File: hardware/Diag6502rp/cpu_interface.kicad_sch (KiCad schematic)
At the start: 23 parts, among them J10 Conn_01x20_PinHeader, J11 Conn_01x20_PinHeader, J6 Conn_02x20_Counter_Clockwise, U4 TXS0108EPWR, U5 TXS0108EPWR, U6 TXS0108EPWR, U7 TXS0108EPWR, U8 TXS0108EPWR

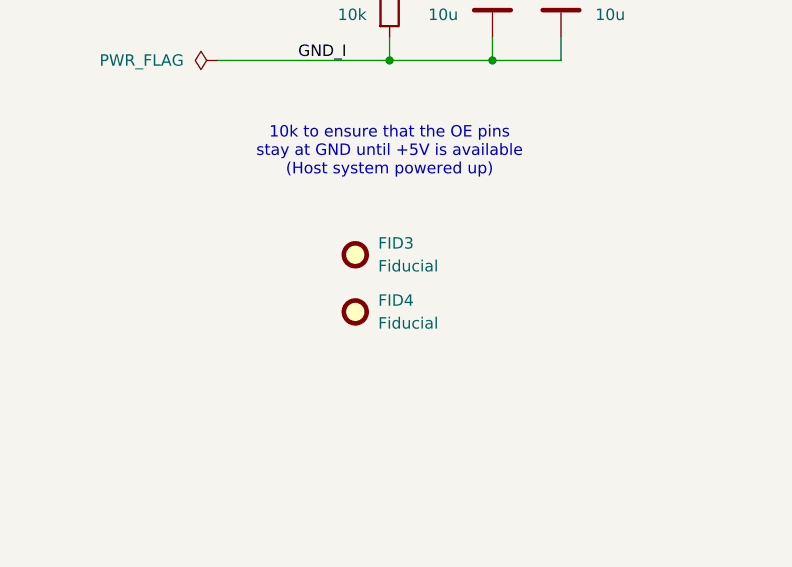
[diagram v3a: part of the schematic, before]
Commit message: More via separation and transfer vias
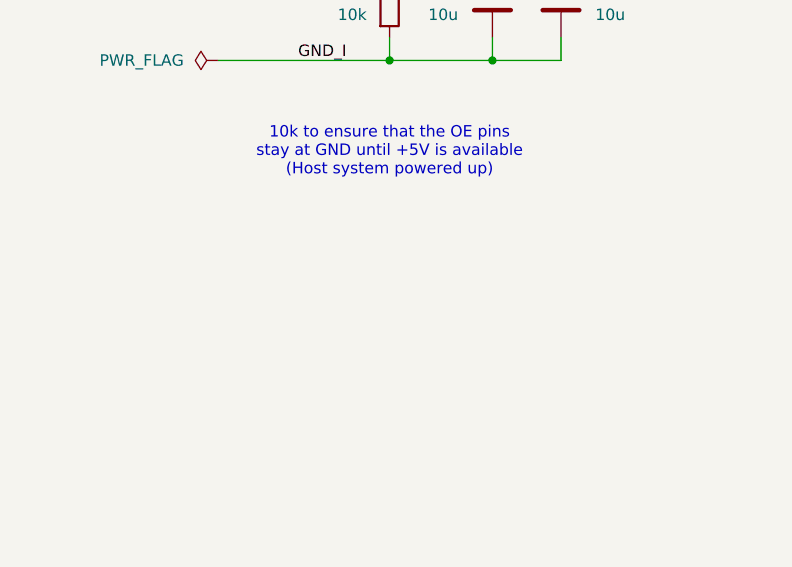
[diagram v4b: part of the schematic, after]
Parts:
- removed FID3, FID4: Fiducial, Fiducial:Fiducial_1mm_Mask2mm, symbol Mechanical:Fiducial
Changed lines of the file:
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@@
-	)
-	(symbol
-		(lib_id "Mechanical:Fiducial")
-		(at 231.14 149.86 0)
-		(unit 1)
-		(exclude_from_sim no)
-		(in_bom no)
-		(on_board yes)
-		(dnp no)
-		(fields_autoplaced yes)
-		(property "Reference" "FID3"
-			(at 233.68 148.5899 0)
-			(effects
-				(font
-					(size 1.27 1.27)
-				)
-				(justify left)
-			)
-		)
-		(property "Value" "Fiducial"
-			(at 233.68 151.1299 0)
-			(effects
-				(font
-					(size 1.27 1.27)
-				)
-				(justify left)
-			)
-		)
-		(property "Footprint" "Fiducial:Fiducial_1mm_Mask2mm"
-			(at 231.14 149.86 0)
-			(effects
-				(font
-					(size 1.27 1.27)
-				)
-				(hide yes)
-			)
-		)
-		(property "Datasheet" "~"
-			(at 231.14 149.86 0)
-			(effects
-				(font
-					(size 1.27 1.27)
-				)
-				(hide yes)
-			)
-		)
-		(property "Description" "Fiducial Marker"
-			(at 231.14 149.86 0)
-			(effects
-				(font
-					(size 1.27 1.27)
-				)
-				(hide yes)
-			)
-		)
-		(instances
-			(project ""
-				(path "/2439caa5-1b7d-40de-b309-64357b0b1cd3/c003db24-4bd6-49ad-8fb6-68dae2466627"
-					(reference "FID3")
-					(unit 1)
-				)
-			)
-		)
 	)
 	(symbol
@@
 					(unit 1)
 				)
-			)
-		)
-	)
-	(symbol
-		(lib_id "Mechanical:Fiducial")
-		(at 231.14 156.21 0)
-		(unit 1)
-		(exclude_from_sim no)
-		(in_bom no)
-		(on_board yes)
-		(dnp no)
-		(fields_autoplaced yes)
-		(property "Reference" "FID4"
-			(at 233.68 154.9399 0)
-			(effects
-				(font
-					(size 1.27 1.27)
-				)
-				(justify left)
-			)
-		)
-		(property "Value" "Fiducial"
-			(at 233.68 157.4799 0)
-			(effects
-				(font
-					(size 1.27 1.27)
-				)
-				(justify left)
-			)
-		)
-		(property "Footprint" "Fiducial:Fiducial_1mm_Mask2mm"
-			(at 231.14 156.21 0)
-			(effects
-				(font
-					(size 1.27 1.27)
-				)
-				(hide yes)
-			)
-		)
-		(property "Datasheet" "~"
-			(at 231.14 156.21 0)
-			(effects
-				(font
-					(size 1.27 1.27)
-				)
-				(hide yes)
-			)
-		)
-		(property "Description" "Fiducial Marker"
-			(at 231.14 156.21 0)
-			(effects
-				(font
-					(size 1.27 1.27)
-				)
-				(hide yes)
-			)
-		)
-		(instances
-			(project ""
-				(path "/2439caa5-1b7d-40de-b309-64357b0b1cd3/c003db24-4bd6-49ad-8fb6-68dae2466627"
-					(reference "FID4")
-					(unit 1)
-				)

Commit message: Rev.A
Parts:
- removed J6: Conn_02x20_Counter_Clockwise, Package_DIP:DIP-40_W15.24mm, symbol Connector_Generic:Conn_02x20_Counter_Clockwise
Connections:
- net +5V_I: now also J11.8 (Pin_8); no longer J11.13 (Pin_13)
- net GND_I: now also J10.20 (Pin_20); no longer J10.1 (Pin_1)
- net PIN_1: now also J11.1 (Pin_1); no longer J11.20 (Pin_20)
- net PIN_10: now also J11.10 (Pin_10); no longer J11.11 (Pin_11)
- net PIN_11: now also J11.11 (Pin_11); no longer J11.10 (Pin_10)
- net PIN_12: now also J11.12 (Pin_12); no longer J11.9 (Pin_9)
- net PIN_13: now also J11.13 (Pin_13); no longer J11.8 (Pin_8)
- net PIN_14: now also J11.14 (Pin_14); no longer J11.7 (Pin_7)
- net PIN_15: now also J11.15 (Pin_15); no longer J11.6 (Pin_6)
- net PIN_16: now also J11.16 (Pin_16); no longer J11.5 (Pin_5)
- net PIN_17: now also J11.17 (Pin_17); no longer J11.4 (Pin_4)
- net PIN_18: now also J11.18 (Pin_18); no longer J11.3 (Pin_3)
- net PIN_19: now also J11.19 (Pin_19); no longer J11.2 (Pin_2)
- net PIN_2: now also J11.2 (Pin_2); no longer J11.19 (Pin_19)
- net PIN_20: now also J11.20 (Pin_20); no longer J11.1 (Pin_1)
- net PIN_22: now also J10.19 (Pin_19); no longer J10.2 (Pin_2)
- net PIN_23: now also J10.18 (Pin_18); no longer J10.3 (Pin_3)
- net PIN_24: now also J10.17 (Pin_17); no longer J10.4 (Pin_4)
- net PIN_25: now also J10.16 (Pin_16); no longer J10.5 (Pin_5)
- net PIN_26: now also J10.15 (Pin_15); no longer J10.6 (Pin_6)
- net PIN_27: now also J10.14 (Pin_14); no longer J10.7 (Pin_7)
- net PIN_28: now also J10.13 (Pin_13); no longer J10.8 (Pin_8)
- net PIN_29: now also J10.12 (Pin_12); no longer J10.9 (Pin_9)
- net PIN_3: now also J11.3 (Pin_3); no longer J11.18 (Pin_18)
- net PIN_30: now also J10.11 (Pin_11); no longer J10.10 (Pin_10)
- net PIN_31: now also J10.10 (Pin_10); no longer J10.11 (Pin_11)
- net PIN_32: now also J10.9 (Pin_9); no longer J10.12 (Pin_12)
- net PIN_33: now also J10.8 (Pin_8); no longer J10.13 (Pin_13)
- net PIN_34: now also J10.7 (Pin_7); no longer J10.14 (Pin_14)
- net PIN_35: now also J10.6 (Pin_6); no longer J10.15 (Pin_15)
- net PIN_36: now also J10.5 (Pin_5); no longer J10.16 (Pin_16)
- net PIN_37: now also J10.4 (Pin_4); no longer J10.17 (Pin_17)
- net PIN_38: now also J10.3 (Pin_3); no longer J10.18 (Pin_18)
- net PIN_39: now also J10.2 (Pin_2); no longer J10.19 (Pin_19)
- net PIN_4: now also J11.4 (Pin_4); no longer J11.17 (Pin_17)
- net PIN_40: now also J10.1 (Pin_1); no longer J10.20 (Pin_20)
- net PIN_5: now also J11.5 (Pin_5); no longer J11.16 (Pin_16)
- net PIN_6: now also J11.6 (Pin_6); no longer J11.15 (Pin_15)
- net PIN_7: now also J11.7 (Pin_7); no longer J11.14 (Pin_14)
- net PIN_9: now also J11.9 (Pin_9); no longer J11.12 (Pin_12)
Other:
- moved on the sheet: J10
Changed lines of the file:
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@@
-	)
-	(symbol
-		(lib_id "Connector_Generic:Conn_02x20_Counter_Clockwise")
-		(at 134.62 138.43 0)
-		(unit 1)
-		(exclude_from_sim no)
-		(in_bom no)
-		(on_board yes)
-		(dnp yes)
-		(fields_autoplaced yes)
-		(property "Reference" "J6"
-			(at 135.89 109.22 0)
-			(effects
-				(font
-					(size 1.27 1.27)
-				)
-			)
-		)
-		(property "Value" "Conn_02x20_Counter_Clockwise"
-			(at 135.89 111.76 0)
-			(effects
-				(font
-					(size 1.27 1.27)
-				)
-			)
-		)
-		(property "Footprint" "Package_DIP:DIP-40_W15.24mm"
-			(at 134.62 138.43 0)
-			(effects
-				(font
-					(size 1.27 1.27)
-				)
-				(hide yes)
-			)
-		)
-		(property "Datasheet" "~"
-			(at 134.62 138.43 0)
-			(effects
-				(font
-					(size 1.27 1.27)
-				)
-				(hide yes)
-			)
-		)
-		(property "Description" "Generic connector, double row, 02x20, counter clockwise pin numbering scheme (similar to DIP package numbering), script generated (kicad-library-utils/schlib/autogen/connector/)"
-			(at 134.62 138.43 0)
-			(effects
-				(font
-					(size 1.27 1.27)
-				)
-				(hide yes)
-			)
-		)
-		(property "LCSC Part #" ""
-			(at 134.62 138.43 0)
-			(effects
-				(font
-					(size 1.27 1.27)
-				)
-				(hide yes)
-			)
-		)
-		(property "Mouser Part #" ""
-			(at 134.62 138.43 0)
-			(effects
-				(font
-					(size 1.27 1.27)
-				)
-				(hide yes)
-			)
-		)
-		(property "LCSC Name" ""
-			(at 134.62 138.43 0)
-			(effects
-				(font
-					(size 1.27 1.27)
-				)
-				(hide yes)
-			)
-		)
-		(pin "8"
-		)
-		(pin "7"
-		)
-		(pin "9"
-		)
-		(pin "21"
-		)
-		(pin "16"
-		)
-		(pin "18"
-		)
-		(pin "30"
-		)
-		(pin "17"
-		)
-		(pin "3"
-		)
-		(pin "38"
-		)
-		(pin "24"
-		)
-		(pin "32"
-		)
-		(pin "5"
-		)
-		(pin "6"
-		)
-		(pin "15"
-		)
-		(pin "40"
-		)
-		(pin "10"
-		)
-		(pin "1"
-		)
-		(pin "11"
-		)
-		(pin "20"
-		)
-		(pin "22"
-		)
-		(pin "23"
-		)
-		(pin "13"
-		)
-		(pin "14"
-		)
-		(pin "12"
-		)
-		(pin "19"
-		)
-		(pin "2"
-		)
-		(pin "25"
-		)
-		(pin "26"
-		)
-		(pin "27"
-		)
-		(pin "28"
-		)
-		(pin "29"
-		)
-		(pin "31"
-		)
-		(pin "34"
-		)
-		(pin "36"
-		)
-		(pin "35"
-		)
-		(pin "37"
-		)
-		(pin "33"
-		)
-		(pin "39"
-		)
-		(pin "4"
-		)
-		(instances
-			(project ""
-				(path "/2439caa5-1b7d-40de-b309-64357b0b1cd3/c003db24-4bd6-49ad-8fb6-68dae2466627"
-					(reference "J6")
-					(unit 1)
-				)
-			)
-		)
 	)
 	(symbol
@@
 	(symbol
 		(lib_id "Connector:Conn_01x20_Pin")
-		(at 111.76 140.97 0)
-		(mirror x)
+		(at 111.76 138.43 0)
 		(unit 1)
 		(exclude_from_sim no)
@@
 		(dnp no)
 		(property "Reference" "J11"
-			(at 110.49 138.4299 0)
+			(at 110.49 140.9701 0)
 			(effects
 				(font
@@
 		)
 		(property "Value" "Conn_01x20_PinHeader"
-			(at 110.49 140.9699 0)
+			(at 110.49 138.4301 0)
 			(effects
 				(font
@@
 		)
 		(property "Footprint" "Connector_PinHeader_2.54mm:PinHeader_1x20_P2.54mm_Vertical"
-			(at 111.76 140.97 0)
+			(at 111.76 138.43 0)
 			(effects
 				(font
@@
 		)
 		(property "Datasheet" "~"
-			(at 111.76 140.97 0)
+			(at 111.76 138.43 0)
 			(effects
 				(font
@@
 		)
 		(property "Description" "Generic connector, single row, 01x20, script generated"
-			(at 111.76 140.97 0)
+			(at 111.76 138.43 0)
 			(effects
 				(font
@@
 		)
 		(property "LCSC Part #" "C50981"
-			(at 111.76 140.97 0)
+			(at 111.76 138.43 0)
 			(effects
 				(font
@@
 		)
 		(property "Mouser Part #" ""
-			(at 111.76 140.97 0)
+			(at 111.76 138.43 0)
 			(effects
 				(font
@@
 		)
 		(property "LCSC Name" ""
-			(at 111.76 140.97 0)
+			(at 111.76 138.43 0)
 			(effects
 				(font
@@
 	(symbol
 		(lib_id "Connector:Conn_01x20_Pin")
-		(at 158.75 140.97 180)
+		(at 158.75 138.43 0)
+		(mirror y)
 		(unit 1)
 		(exclude_from_sim no)
@@
 		(on_board yes)
 		(dnp no)
-		(fields_autoplaced yes)
 		(property "Reference" "J10"
-			(at 160.02 138.4299 0)
+			(at 160.02 140.9701 0)
 			(effects
 				(font
@@
 		)
 		(property "Value" "Conn_01x20_PinHeader"
-			(at 160.02 140.9699 0)
+			(at 160.02 138.4301 0)
 			(effects
 				(font
@@
 		)
 		(property "Footprint" "Connector_PinHeader_2.54mm:PinHeader_1x20_P2.54mm_Vertical"
-			(at 158.75 140.97 0)
+			(at 158.75 138.43 0)
 			(effects
 				(font
@@
 		)
 		(property "Datasheet" "~"
-			(at 158.75 140.97 0)
+			(at 158.75 138.43 0)
 			(effects
 				(font
@@
 		)
 		(property "Description" "Generic connector, single row, 01x20, script generated"
-			(at 158.75 140.97 0)
+			(at 158.75 138.43 0)
 			(effects
 				(font
@@
 		)
 		(property "LCSC Part #" "C50981"
-			(at 158.75 140.97 0)
+			(at 158.75 138.43 0)
 			(effects
 				(font
@@
 		)
 		(property "Mouser Part #" ""
-			(at 158.75 140.97 0)
+			(at 158.75 138.43 0)
 			(effects
 				(font
@@
 		)
 		(property "LCSC Name" ""
-			(at 158.75 140.97 0)
-			(effects
-				(font
+			(at 158.75 138.43 0)
+			(effects
+				(font
